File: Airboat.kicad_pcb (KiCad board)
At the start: 2 copper layers, 100 x 100 mm, 46 parts, among them J1 USB_B_Micro, J2 Barrel_Jack_Switch_Pin3Ring, J3 Screw_Terminal_01x02, J5 Screw_Terminal_01x02, Q1 BC818, Q2 BC818, SW1 SW_Omron_B3FS, SW3 SW_Omron_B3FS, U1 ESP32-WROOM-32E, U2 CP2102N-Axx-xQFN28, U3 AP2127N-3.3, U5 L293D, X1 SG-3030CM

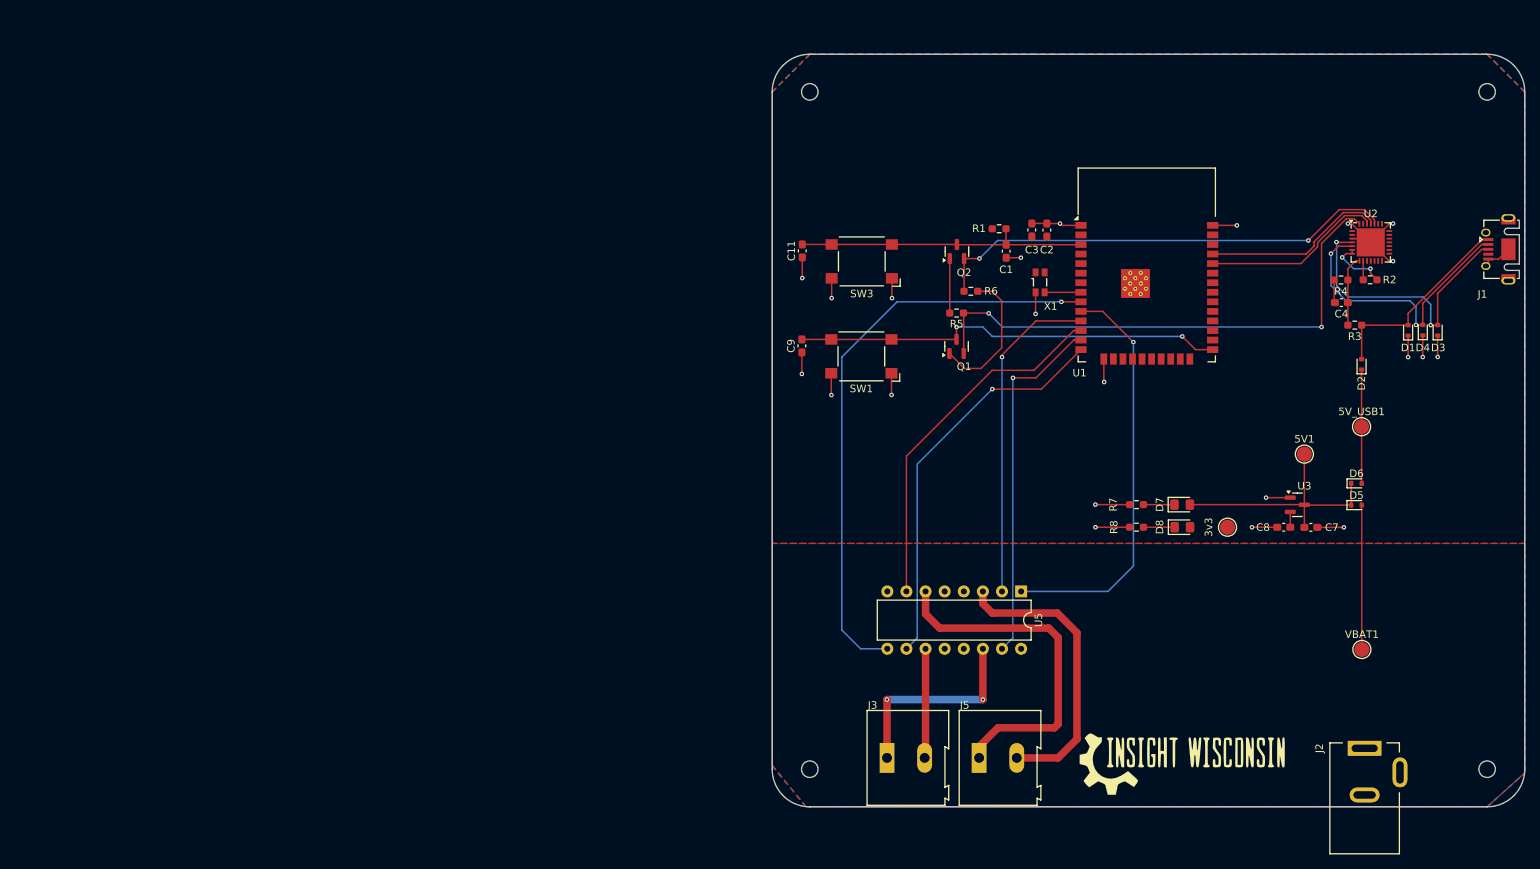
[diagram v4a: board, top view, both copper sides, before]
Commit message: Updated PCB to be smaller and support stepper
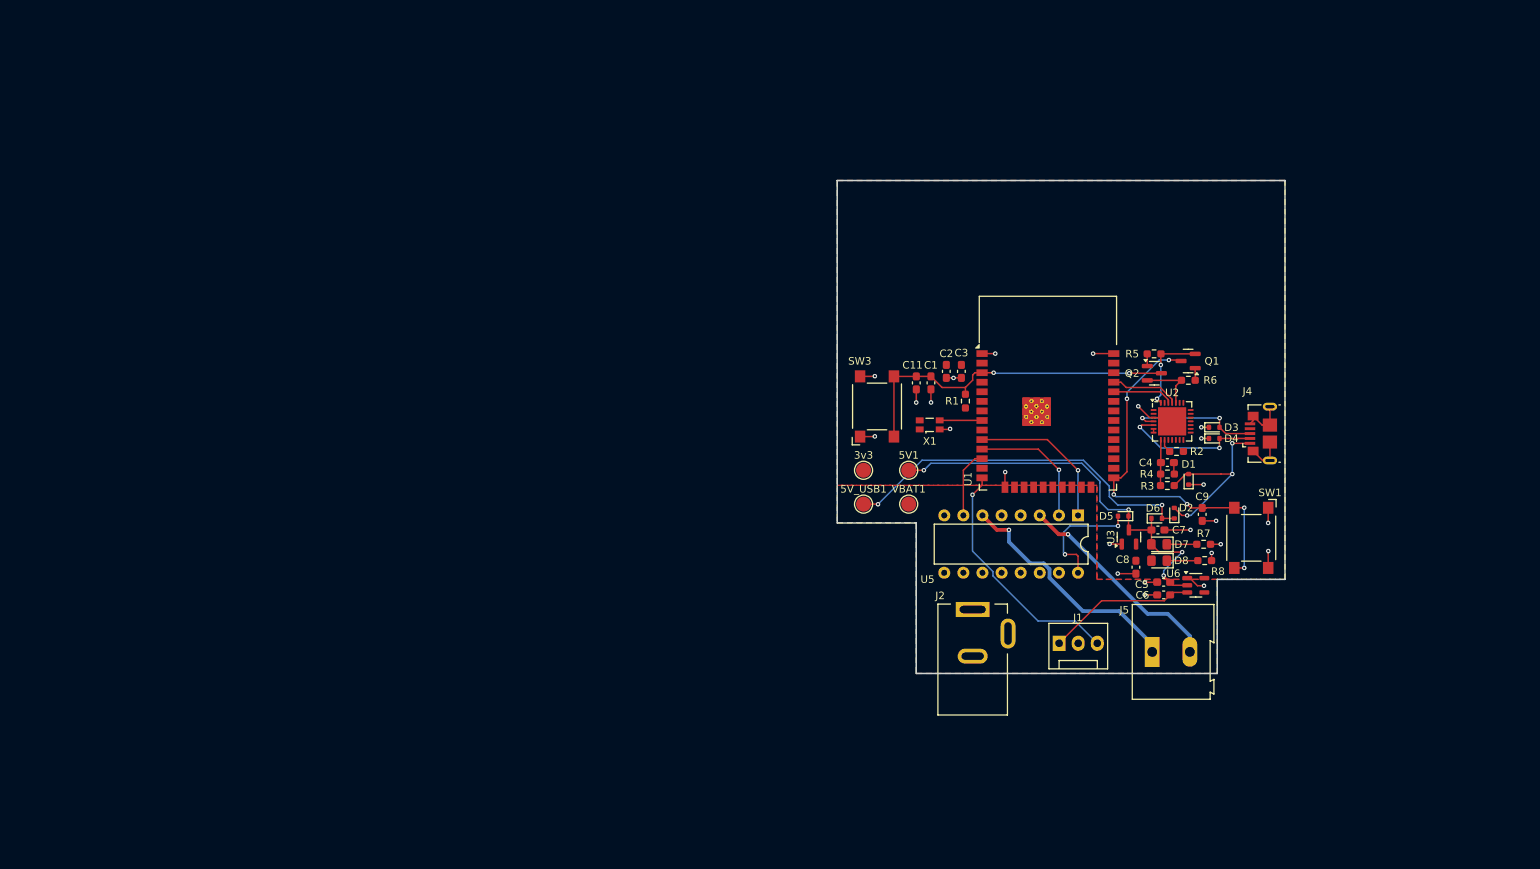
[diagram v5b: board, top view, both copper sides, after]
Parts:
- removed H1, H2, H3, H5: MountingHole, MountingHole:MountingHole_2.2mm_M2
- removed J3: Screw_Terminal_01x02, TerminalBlock:TerminalBlock_Altech_AK300-2_P5.00mm
- removed L1: ~, Insight Logo:Insight_Logo
- added C5: 1uF, Capacitor_SMD:C_0603_1608Metric_Pad1.08x0.95mm_HandSolder, F.Cu at (152.0, 120.2)
- added C6: 1uF, Capacitor_SMD:C_0603_1608Metric_Pad1.08x0.95mm_HandSolder, F.Cu at (152.0, 121.8)
- added J4: USB_B_Micro, Connector_USB:USB_Micro-B_GCT_USB3076-30-A, F.Cu at (164.9, 100.4)
- added U6: MC78LC50NTR, Package_TO_SOT_SMD:SOT-23-5, F.Cu at (156.3, 120.6)
- J1: value USB_B_Micro -> Conn_01x03_Pin; footprint Connector_USB:USB_Micro-AB_Molex_47590-0001 -> Connector:FanPinHeader_1x03_P2.54mm_Vertical
- moved J1 79.4 mm to (138.1, 128.3), turned to 0 degrees
- moved 5V_USB1 67.0 mm to (112.1, 109.8)
- moved VBAT1 63.2 mm to (118.1, 109.8)
- moved C9 57.7 mm to (157.1, 111.1)
- moved SW1 57.1 mm to (163.7, 114.3), turned to -90 degrees
- moved J2 55.2 mm to (126.6, 123.8)
- moved 5V1 52.6 mm to (118.1, 105.3)
- moved 3v3 49.0 mm to (112.1, 105.3), turned to 0 degrees
- moved U2 35.5 mm to (153.1, 98.8)
- moved D1 35.2 mm to (155.3, 106.5)
- moved R4 34.6 mm to (152.5, 105.8), turned to 0 degrees
- moved R2 34.4 mm to (153.7, 102.8)
- moved R3 32.8 mm to (152.5, 107.3)
- moved D3 32.4 mm to (158.7, 99.6), turned to 0 degrees
- moved D2 31.8 mm to (153.4, 111.0)
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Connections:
- J1 pad 1: +VBUS -> +5V
- J1 pad 2: USB_DM -> GND
- J1 pad 3: USB_DP -> RUDDER_SIG
- U1 pad 13: RUDDER_B -> unconnected-(U1-IO14-Pad13)
- U1 pad 14: RUDDER_F -> RUDDER_SIG
- U1 pad 9: RUDDER_PWM -> unconnected-(U1-IO33-Pad9)
- U5 pad 10: RUDDER_F -> unconnected-(U5-3A-Pad10)
- U5 pad 11: RUDDER_POS -> unconnected-(U5-3Y-Pad11)
- U5 pad 14: RUDDER_NEG -> unconnected-(U5-4Y-Pad14)
- U5 pad 15: RUDDER_B -> unconnected-(U5-4A-Pad15)
- U5 pad 9: RUDDER_PWM -> unconnected-(U5-EN3,4-Pad9)
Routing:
- net RUDDER_PWM: track 78.2 -> 0.00 mm, vias 1 -> 0
- net DTR: track 71.5 -> 11.5 mm
- net RTS: track 62.7 -> 7.85 mm, vias 2 -> 0
- net RUDDER_F: track 53.2 -> 0.00 mm, vias 1 -> 0
- net RUDDER_B: track 48.4 -> 0.00 mm, vias 1 -> 0
- net FAN_B: track 48.1 -> 9.12 mm
- net FAN_PWM: track 54.7 -> 20.4 mm
- net +5_USB: track 15.1 -> 48.8 mm, vias 0 -> 2
- net RUDDER_SIG: track 0.00 -> 32.3 mm, vias 0 -> 1
- net RUDDER_NEG: track 27.3 -> 0.00 mm, vias 2 -> 0
- net FAN_F: track 43.8 -> 17.4 mm
- net +V_MCU: track 34.1 -> 55.3 mm, vias 0 -> 4
- net GND: track 81.2 -> 60.3 mm, vias 22 -> 24
- net USB_DP: track 38.5 -> 17.6 mm
- net +5V: track 0.00 -> 19.8 mm
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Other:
- board size 100 x 100 mm -> 59.5 x 65.5 mm

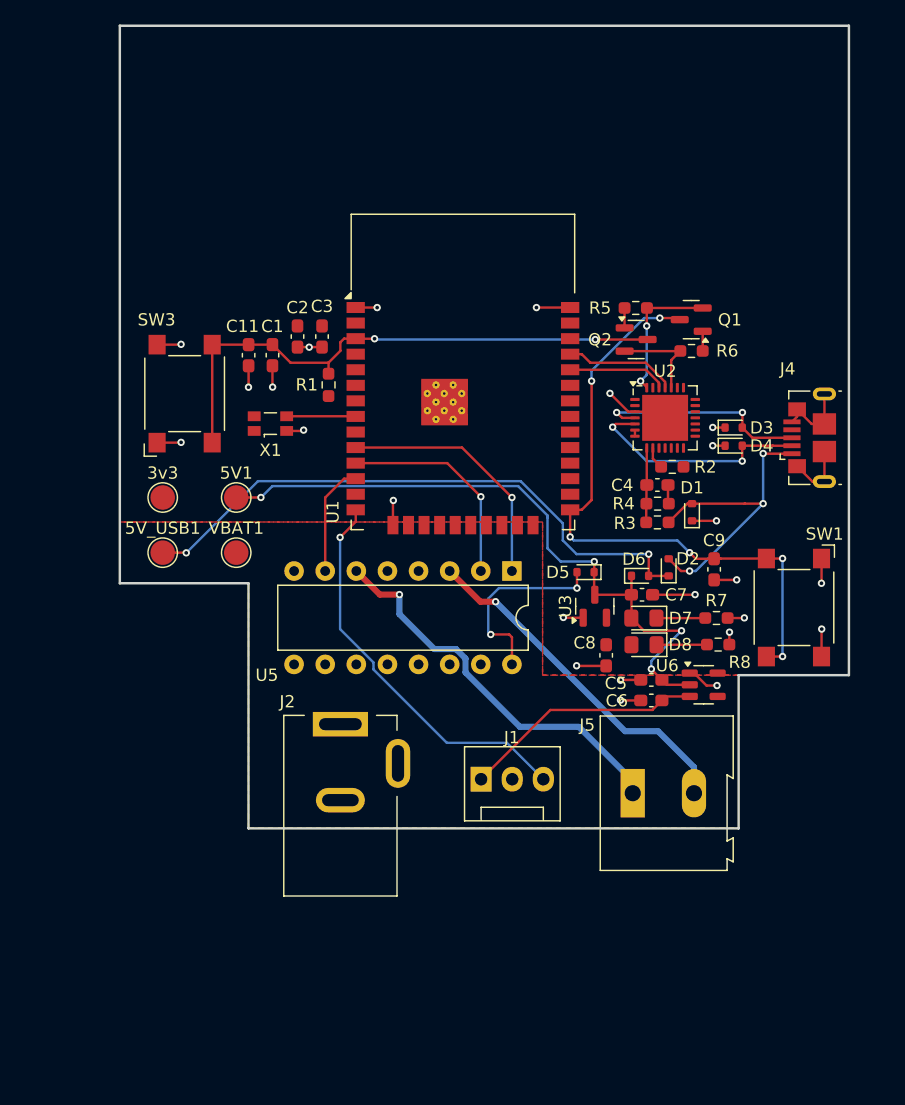
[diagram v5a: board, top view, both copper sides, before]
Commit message: Updated to use boost converters
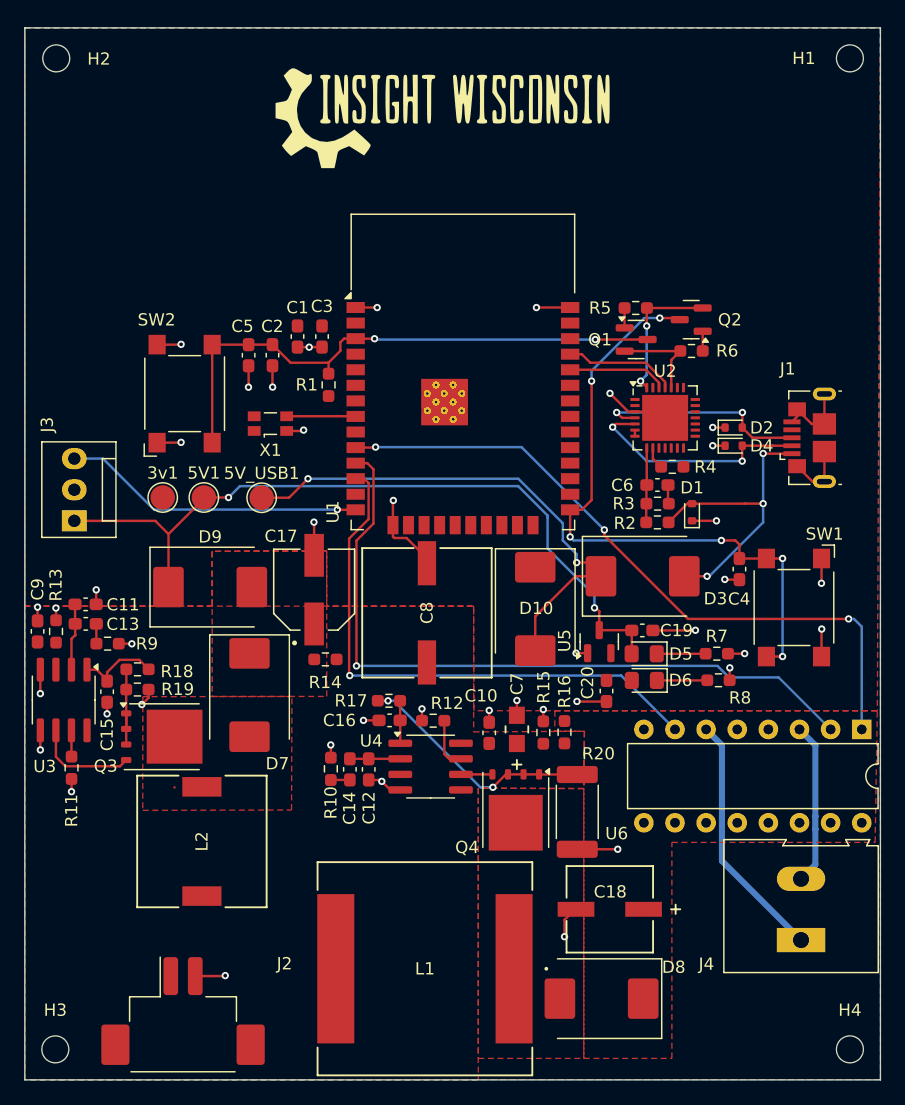
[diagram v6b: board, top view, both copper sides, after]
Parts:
- removed the C5 at (152.0, 120.2)
- removed the C6 at (152.0, 121.8)
- removed the D2 at (153.4, 111.0)
- removed the D5 at (146.6, 111.4)
- removed the D6 at (151.1, 111.7)
- removed the U6 at (156.3, 120.6)
- removed VBAT1: VBAT_TP, TestPoint:TestPoint_Pad_D2.0mm
- added C10: 100nF, Capacitor_SMD:C_0603_1608Metric_Pad1.08x0.95mm_HandSolder, F.Cu at (138.8, 124.5)
- added C11: 1nF, Capacitor_SMD:C_0603_1608Metric_Pad1.08x0.95mm_HandSolder, F.Cu at (105.9, 114.0)
- added C12: 12nF, Capacitor_SMD:C_0603_1608Metric_Pad1.08x0.95mm_HandSolder, F.Cu at (129.0, 127.5)
- added C13: 18nF, Capacitor_SMD:C_0603_1608Metric_Pad1.08x0.95mm_HandSolder, F.Cu at (105.9, 115.6)
- added C14: 220nF, Capacitor_SMD:C_0603_1608Metric_Pad1.08x0.95mm_HandSolder, F.Cu at (127.4, 127.5)
- added C15: 56pF, Capacitor_SMD:C_0603_1608Metric_Pad1.08x0.95mm_HandSolder, F.Cu at (107.6, 121.1)
- added C16: 56pF, Capacitor_SMD:C_0603_1608Metric_Pad1.08x0.95mm_HandSolder, F.Cu at (130.7, 123.5)
- added C17: 16SVPG270M, Insight:CAP_16SVPG270M, F.Cu at (124.5, 112.8)
- added C18: 20SVPF120M, Insight:PCAP_SVP_C6_PAN, F.Cu at (148.6, 138.9)
- added C7: T520A107M006ATE025, Insight:CAPMP3.4X1.6_1.8N_KEM, F.Cu at (141.0, 124.2)
- added C8: UUD1E471MNL1GS, Insight:U2-R_NCH, F.Cu at (133.7, 114.7)
- added C9: 100nF, Capacitor_SMD:C_0603_1608Metric_Pad1.08x0.95mm_HandSolder, F.Cu at (101.9, 116.2)
- added D10: D_Schottky, Diode_SMD:D_SMC, F.Cu at (142.5, 114.4)
- added D3: D_Schottky, Diode_SMD:D_SMC, F.Cu at (151.3, 111.7)
- added D7: D_Schottky, Diode_SMD:D_SMC, F.Cu at (119.2, 121.4)
- added D8: D_Schottky, Diode_SMD:D_SMC, F.Cu at (148.0, 146.2)
- added D9: D_Schottky, Diode_SMD:D_SMC, F.Cu at (116.0, 112.6)
- added H1: MountingHole, MountingHole:MountingHole_2.2mm_M2, F.Cu at (168.2, 69.4)
- added H2: MountingHole, MountingHole:MountingHole_2.2mm_M2, F.Cu at (103.5, 69.4)
- added H3: MountingHole, MountingHole:MountingHole_2.2mm_M2, F.Cu at (103.4, 150.3)
- added H4: MountingHole, MountingHole:MountingHole_2.2mm_M2, F.Cu at (168.2, 150.3)
- added L1: IHLP6767GZER3R3M51, Insight:IND_IHLP-6767GZ_VIS, F.Cu at (133.5, 143.7)
- added L2: DR1040-1R5-R, Insight:DR1040, F.Cu at (115.3, 133.3)
- added LOGO1: ~, Insight:Insight_Logo, F.Cu at (136.0, 74.0)
- added Q3: CSD16321Q5, Package_TO_SOT_SMD:TDSON-8-1, F.Cu at (112.1, 124.8)
- added Q4: CSD16321Q5, Package_TO_SOT_SMD:TDSON-8-1, F.Cu at (141.0, 130.8)
- added R10: 1kOhm, Resistor_SMD:R_0603_1608Metric_Pad0.98x0.95mm_HandSolder, F.Cu at (125.9, 127.4)
- added R11: 17.4kOhm, Resistor_SMD:R_0603_1608Metric_Pad0.98x0.95mm_HandSolder, F.Cu at (104.7, 127.3)
- added R12: 75kOhm, Resistor_SMD:R_0603_1608Metric_Pad0.98x0.95mm_HandSolder, F.Cu at (134.2, 123.5)
- added R13: 1kOhm, Resistor_SMD:R_0603_1608Metric_Pad0.98x0.95mm_HandSolder, F.Cu at (103.4, 116.2)
- added R14: 2.94kOhm, Resistor_SMD:R_0603_1608Metric_Pad0.98x0.95mm_HandSolder, F.Cu at (125.4, 118.5)
- added R15: 1kOhm, Resistor_SMD:R_0603_1608Metric_Pad0.98x0.95mm_HandSolder, F.Cu at (143.2, 124.5)
- added R16: 8.45kOhm, Resistor_SMD:R_0603_1608Metric_Pad0.98x0.95mm_HandSolder, F.Cu at (144.9, 124.4)
- added R17: 0.1kOhm, Resistor_SMD:R_0603_1608Metric_Pad0.98x0.95mm_HandSolder, F.Cu at (130.6, 121.9)
- added R18: 0.1kOhm, Resistor_SMD:R_0603_1608Metric_Pad0.98x0.95mm_HandSolder, F.Cu at (110.1, 119.3)
- added R19: 12mOhm, Resistor_SMD:R_0603_1608Metric_Pad0.98x0.95mm_HandSolder, F.Cu at (110.1, 121.0)
- added R20: 3.3mOhm, Resistor_SMD:R_2512_6332Metric_Pad1.40x3.35mm_HandSolder, F.Cu at (146.0, 130.9)
- added R9: 2.67kOhm, Resistor_SMD:R_0603_1608Metric_Pad0.98x0.95mm_HandSolder, F.Cu at (107.6, 117.2)
- added U3: LM3478MA, Package_SO:SOIC-8_3.9x4.9mm_P1.27mm, F.Cu at (104.1, 121.8)
- added U4: LM3478MA, Package_SO:SOIC-8_3.9x4.9mm_P1.27mm, F.Cu at (134.0, 127.2)
- J2: value Barrel_Jack_Switch_Pin3Ring -> Conn_01x02_MountingPin; footprint Connector_BarrelJack:BarrelJack_Kycon_KLDX-0202-xC_Horizontal -> Connector_Hirose:Hirose_DF3EA-02P-2H_1x02-1MP_P2.00mm_Horizontal
- R7: value 330R -> 330Ohm
- R8: value 330kR -> 330Ohm
- moved J3 39.3 mm to (104.9, 107.2), turned to 90 degrees
- moved U6 31.3 mm to (169.2, 124.2)
- moved J2 26.7 mm to (113.8, 147.2), turned to 0 degrees
- moved J4 18.2 mm to (164.2, 141.4), turned to 90 degrees
- moved 5V_USB1 9.24 mm to (120.2, 105.3)
- moved U5 2.91 mm to (147.8, 117.0)
- moved C19 2.91 mm to (151.3, 116.1)
- moved C20 2.91 mm to (148.4, 121.1)
- moved D5 2.91 mm to (151.4, 118.0)
- moved D6 2.91 mm to (151.4, 120.2)
- moved R8 2.91 mm to (157.5, 120.2)
- moved R7 2.91 mm to (157.4, 118.0)
- moved 5V1 2.64 mm to (115.5, 105.3)
- moved C4 2.06 mm to (159.2, 111.1)
- renumbered 3v3 to 3v1, C2 to C1, C7 to C19, C1 to C2, C8 to C20, C9 to C4, C11 to C5, C4 to C6, D3 to D2, D7 to D5, D8 to D6, J4 to J1, J1 to J3, J5 to J4, Q2 to Q1, Q1 to Q2, R3 to R2, R4 to R3, R2 to R4, SW3 to SW2, U3 to U5, U5 to U6
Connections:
- J3 pad 1: +5V -> +V_MCU
- U6 pad 14: unconnected-(U5-4Y-Pad14) -> (no net)
- U6 pad 16: +BATT -> +12V
- U6 pad 8: +BATT -> +12V
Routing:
- net FAN_F: track 17.4 -> 59.1 mm
- net FAN_B: track 9.12 -> 45.9 mm, vias 0 -> 1
- net FAN_PWM: track 20.4 -> 56.0 mm, vias 1 -> 3
- net GND: track 60.3 -> 89.7 mm, vias 24 -> 41
- net +5V: track 19.8 -> 0.00 mm
- net /Power/12V_MOS_S: track 0.00 -> 19.6 mm, vias 0 -> 2
- net +BATT: track 15.9 -> 0.00 mm, vias 2 -> 0
- net FAN_POS: track 28.7 -> 13.2 mm, vias 1 -> 0
- net FAN_NEG: track 32.3 -> 20.4 mm, vias 1 -> 0
- net /Power/5V_LM_DR: track 0.00 -> 8.43 mm
- net RUDDER_SIG: track 32.3 -> 24.7 mm
- net /Power/5V_MOS_S: track 0.00 -> 7.41 mm
- net /Power/5V_LM_SEN: track 0.00 -> 6.94 mm
- net +V_MCU: track 55.3 -> 61.8 mm, vias 4 -> 2
- net +5_USB: track 48.8 -> 42.4 mm
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- added copper zone on F.Cu, net +12V
- added copper zone on F.Cu, net +5V_Boost
- added copper zone on F.Cu, net /Power/12V_MOS_D
- added copper zone on F.Cu, net /Power/5V_MOS_D
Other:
- board size 59.5 x 65.5 mm -> 69.8 x 85.9 mm
